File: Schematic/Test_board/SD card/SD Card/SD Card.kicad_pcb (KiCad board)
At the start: 2 copper layers, 10 parts, among them J1 Conn_01x07_Female, J3 Conn_01x05_Female, J4 503398-1892, U2 ICM-20602, U3 TXB0104PW

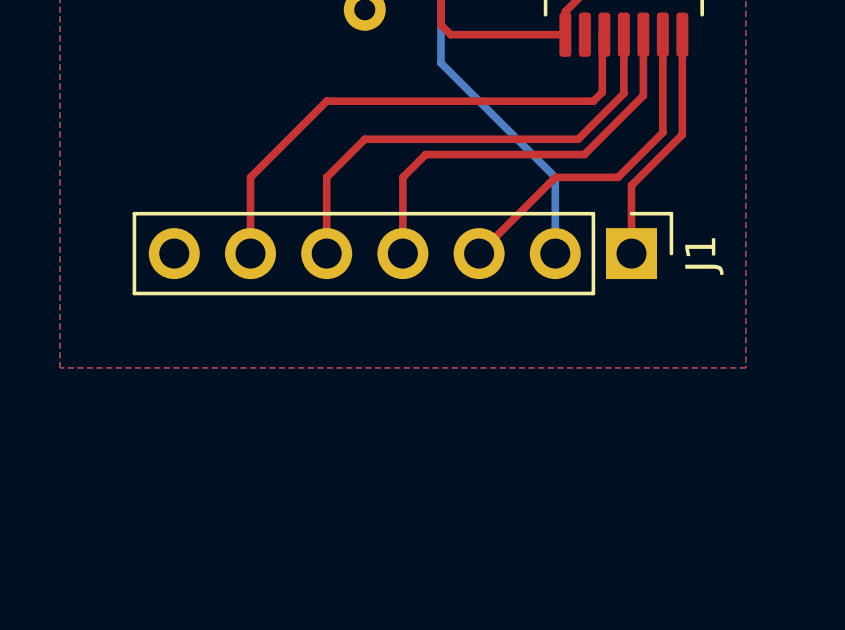
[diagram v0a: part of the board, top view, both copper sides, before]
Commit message: test board PCB design
PCB includes SD card and IMU

2.2 Basic Sensor Suite
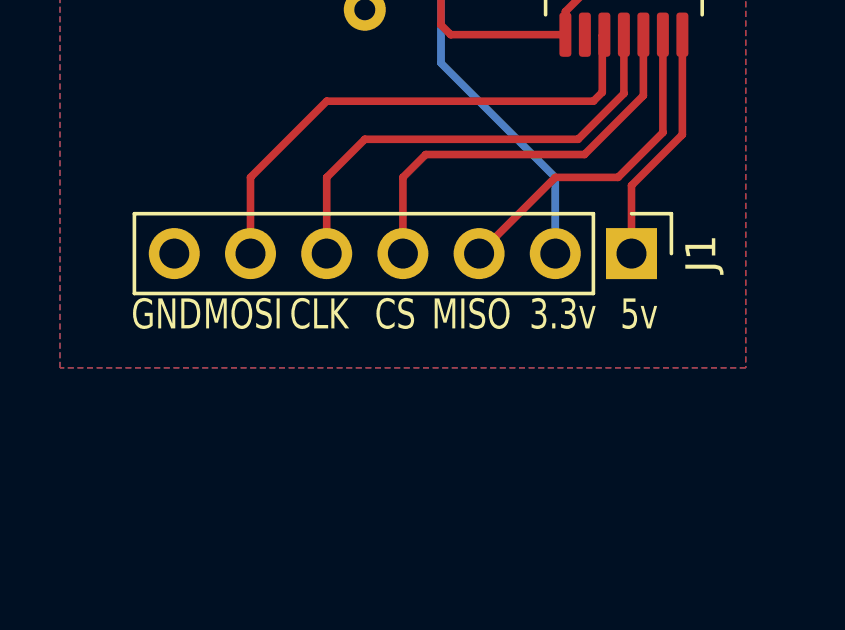
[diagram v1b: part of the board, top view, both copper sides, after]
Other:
- board text added: "3.3v"
- board text added: "5v"
- board text added: "CLK"
- board text added: "CS"
- board text added: "GND"
- board text added: "MISO"
- board text added: "MOSI"

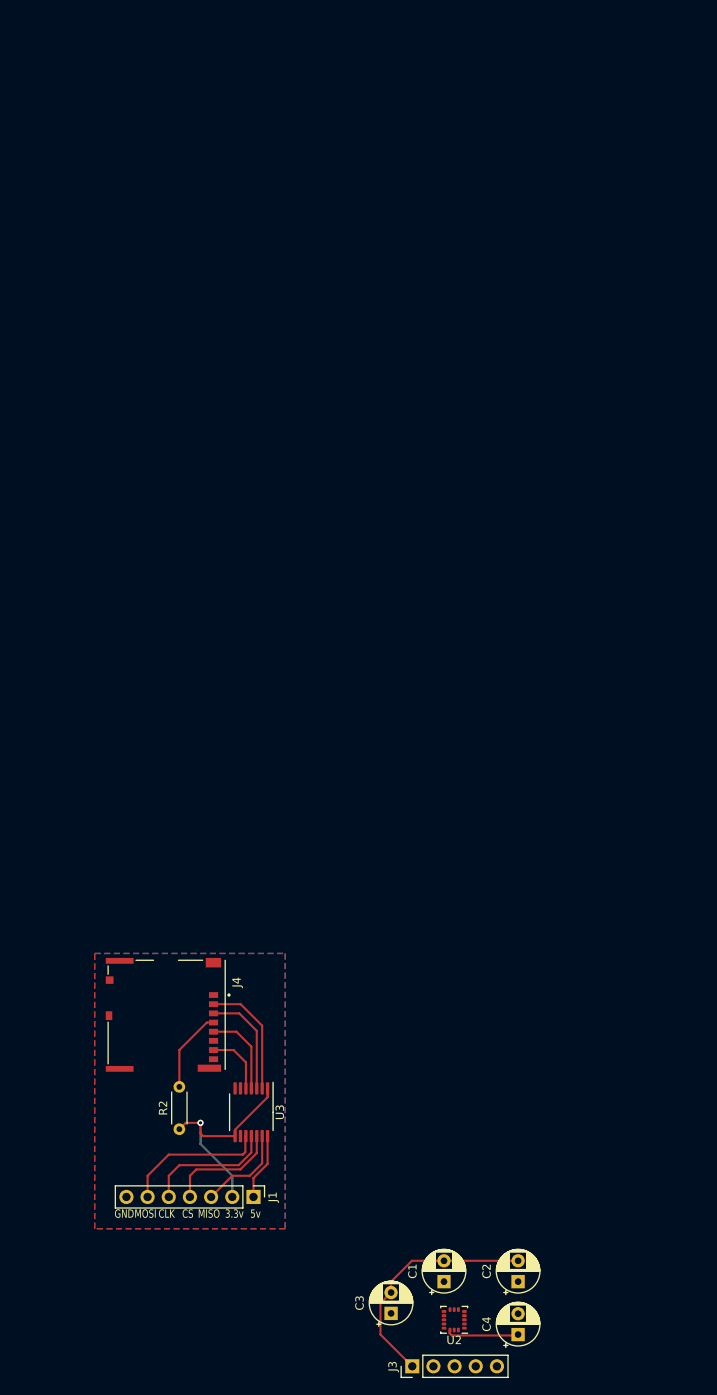
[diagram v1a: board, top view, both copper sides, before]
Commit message: Test board PCB design
Board includes SD card, IMU and PDU

2.2 Basic Sensor Suite
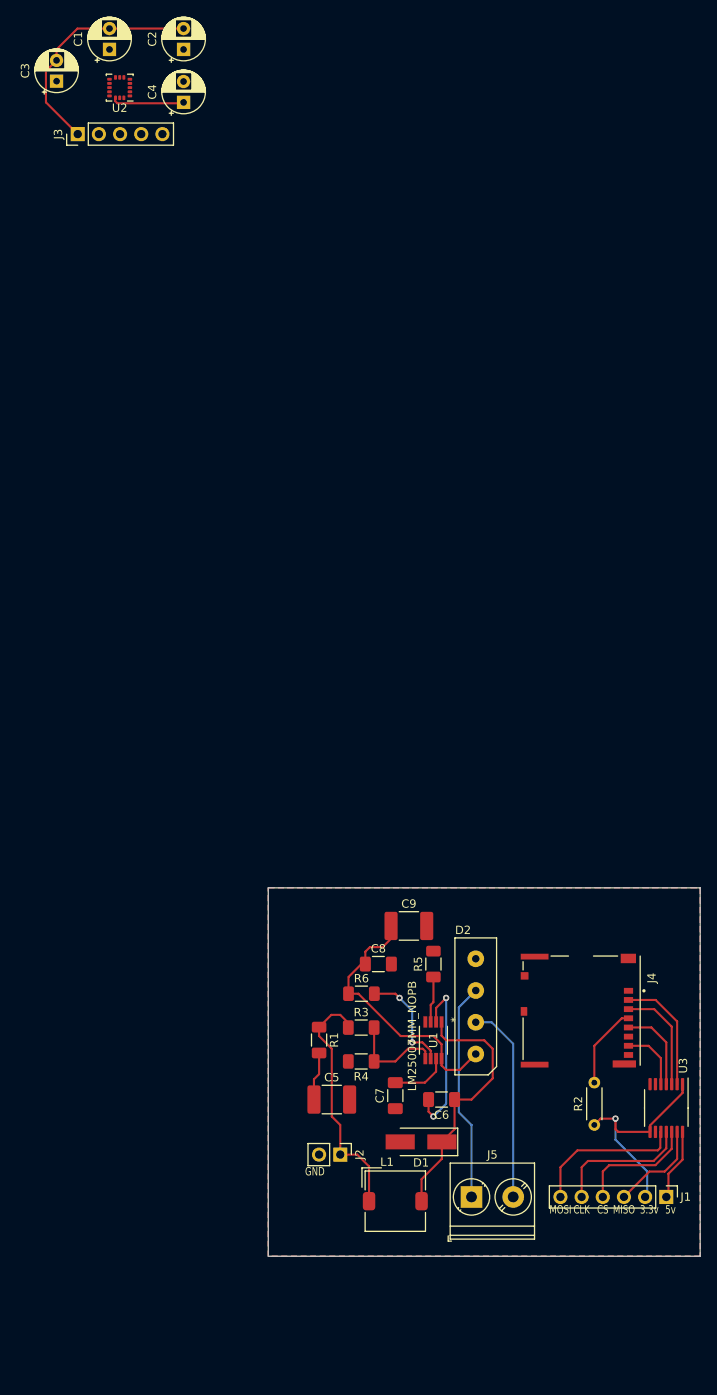
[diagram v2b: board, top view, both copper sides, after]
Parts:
- added C5: 15uF, Capacitor_SMD:C_1812_4532Metric_Pad1.57x3.40mm_HandSolder, F.Cu at (51.3, 145.8)
- added C6: 0.01uF, Capacitor_SMD:C_1206_3216Metric_Pad1.33x1.80mm_HandSolder, F.Cu at (64.5, 145.8)
- added C7: 0.1uF, Capacitor_SMD:C_1206_3216Metric_Pad1.33x1.80mm_HandSolder, F.Cu at (58.9, 145.3)
- added C8: 0.1uF, Capacitor_SMD:C_1206_3216Metric_Pad1.33x1.80mm_HandSolder, F.Cu at (56.9, 129.5)
- added C9: 1uF, Capacitor_SMD:C_1812_4532Metric_Pad1.57x3.40mm_HandSolder, F.Cu at (60.6, 125.0)
- added D1: D, Diode_SMD:D_SMA_Handsoldering, F.Cu at (62.0, 150.9)
- added D2: D_Bridge_+AA-, TTS_UART:KBP306GTB, F.Cu at (68.6, 134.6)
- added J2: Conn_01x02_Female, Connector_PinHeader_2.54mm:PinHeader_1x02_P2.54mm_Vertical, F.Cu at (52.3, 152.4)
- added J5: Screw_Terminal_01x02, TerminalBlock_Phoenix:TerminalBlock_Phoenix_PT-1,5-2-5.0-H_1x02_P5.00mm_Horizontal, F.Cu at (68.1, 157.5)
- added L1: 100uH, Inductor_SMD:L_TDK_SLF7045, F.Cu at (58.9, 158.0)
- added R1: 1, Resistor_SMD:R_1206_3216Metric_Pad1.30x1.75mm_HandSolder, F.Cu at (49.8, 138.7)
- added R3: 3.01k, Resistor_SMD:R_1206_3216Metric_Pad1.30x1.75mm_HandSolder, F.Cu at (54.8, 137.2)
- added R4: 1k, Resistor_SMD:R_1206_3216Metric_Pad1.30x1.75mm_HandSolder, F.Cu at (54.8, 141.2)
- added R5: 100k, Resistor_SMD:R_1206_3216Metric_Pad1.30x1.75mm_HandSolder, F.Cu at (63.5, 129.5)
- added R6: 200k, Resistor_SMD:R_1206_3216Metric_Pad1.30x1.75mm_HandSolder, F.Cu at (54.9, 133.1)
- added U1: LM25007MM_NOPB, LM25007MM:LM25007MM&slash_NOPB, F.Cu at (63.5, 138.7)
- J1: value Conn_01x07_Female -> Conn_01x06_Female; footprint Connector_PinHeader_2.54mm:PinHeader_1x07_P2.54mm_Vertical -> Connector_PinHeader_2.54mm:PinHeader_1x06_P2.54mm_Vertical
- moved C3 153.2 mm to (18.3, 23.6)
- moved C4 153.2 mm to (33.5, 26.2)
- moved J3 153.2 mm to (20.8, 30.0)
- moved U2 153.2 mm to (25.9, 24.4)
- moved C1 153.2 mm to (24.6, 19.8)
- moved C2 153.2 mm to (33.5, 19.8)
- moved J4 49.8 mm to (81.3, 135.1)
- moved R2 49.8 mm to (82.8, 148.8)
- moved U3 49.8 mm to (91.4, 146.8)
- moved J1 49.5 mm to (91.4, 157.5)
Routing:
- net Net-(C8-Pad1): track 0.00 -> 32.7 mm
- net Net-(C6-Pad1): track 0.00 -> 31.4 mm
- net Net-(J2-Pad1): track 0.00 -> 29.6 mm
- net Net-(D2-Pad3): track 0.00 -> 26.2 mm
- net Net-(D2-Pad2): track 0.00 -> 23.9 mm
- net /BST: track 0.00 -> 20.5 mm, vias 0 -> 2
- net /RON: track 0.00 -> 12.8 mm, vias 0 -> 2
- net /FB: track 0.00 -> 11.8 mm
- net Net-(C7-Pad2): track 0.00 -> 6.99 mm
- net Net-(C5-Pad1): track 0.00 -> 5.84 mm
- net Net-(R5-Pad1): track 0.00 -> 5.53 mm
- net Net-(J1-Pad5): track 15.6 -> 16.6 mm
- net Net-(J1-Pad4): track 13.7 -> 14.5 mm
- net /5v: track 8.00 -> 8.61 mm
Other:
- board outline added: 51.8 x 44.2 mm
- board text added: "TEST BOARD v00"
